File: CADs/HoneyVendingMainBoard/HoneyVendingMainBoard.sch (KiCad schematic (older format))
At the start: 31 parts, among them J1 SegmentPins, J2 CoinPins, J3 ConnToDoors, J4 12V Power, U1 L7805, U2 74HC165

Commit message: Update mainboard schematic
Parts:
- added 10kOhm? (x2): R, Resistor_SMD:R_0805_2012Metric_Pad1.15x1.40mm_HandSolder, symbol Device:R
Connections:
- net CoinSerial: now also 10kOhm?.1
- net GND: now also 10kOhm?.2, 10kOhm?.2
- net PISOOutput: now also 10kOhm?.1
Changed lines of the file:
@@
 	1    0    0    -1
 $EndComp
-Text Notes 3550 3500 0    50   ~ 0
+Text Notes 3550 3450 0    50   ~ 0
 Pins 2 and 3 are \ncapable of interrupts
 $Comp
@@
 	4350 3700 5100 3700
 Wire Wire Line
-	4350 3600 5100 3600
-Wire Wire Line
 	4350 3800 5100 3800
 Wire Wire Line
-	4350 3900 5100 3900
-Wire Wire Line
 	4350 4000 5100 4000
 Wire Wire Line
@@
 Wire Wire Line
 	4350 4600 5100 4600
-Text Label 4350 3600 0    50   ~ 0
+Text Label 4000 3600 0    50   ~ 0
 CoinSerial
 Text Label 4350 3700 0    50   ~ 0
@@
 Text Label 4350 3800 0    50   ~ 0
 PISOClock
-Text Label 4350 3900 0    50   ~ 0
+Text Label 3650 3900 0    50   ~ 0
 PISOOutput
 Text Label 4350 4000 0    50   ~ 0
@@
 Text Notes 4450 4650 0    20   ~ 0
 Pin 13 reserviert für Coin TX
+Wire Wire Line
+	4000 3600 4500 3600
+$Comp
+L Device:R 10kOhm?
+U 1 1 5E8354F3
+P 4300 3050
+F 0 "10kOhm?" V 4093 3050 50  0000 C CNN
+F 1 "R" V 4184 3050 50  0000 C CNN
+F 2 "Resistor_SMD:R_0805_2012Metric_Pad1.15x1.40mm_HandSolder" V 4230 3050 50  0001 C CNN
+F 3 "~" H 4300 3050 50  0001 C CNN
+	1    4300 3050
+	0    1    1    0
+$EndComp
+$Comp
+L power:GND #PWR?
+U 1 1 5E835551
+P 4000 3050
+F 0 "#PWR?" H 4000 2800 50  0001 C CNN
+F 1 "GND" H 4005 2877 50  0000 C CNN
+F 2 "" H 4000 3050 50  0001 C CNN
+F 3 "" H 4000 3050 50  0001 C CNN
+	1    4000 3050
+	0    1    1    0
+$EndComp
+Wire Wire Line
+	4150 3050 4000 3050
+Wire Wire Line
+	4450 3050 4500 3050
+Wire Wire Line
+	4500 3050 4500 3600
+Connection ~ 4500 3600
+Wire Wire Line
+	4500 3600 5100 3600
+$Comp
+L Device:R 10kOhm?
+U 1 1 5E8476D8
+P 3700 3700
+F 0 "10kOhm?" V 3493 3700 50  0000 C CNN
+F 1 "R" V 3584 3700 50  0000 C CNN
+F 2 "Resistor_SMD:R_0805_2012Metric_Pad1.15x1.40mm_HandSolder" V 3630 3700 50  0001 C CNN
+F 3 "~" H 3700 3700 50  0001 C CNN
+	1    3700 3700
+	0    1    1    0
+$EndComp
+$Comp
+L power:GND #PWR?
+U 1 1 5E847732
+P 3450 3700
+F 0 "#PWR?" H 3450 3450 50  0001 C CNN
+F 1 "GND" H 3455 3527 50  0000 C CNN
+F 2 "" H 3450 3700 50  0001 C CNN
+F 3 "" H 3450 3700 50  0001 C CNN
+	1    3450 3700
+	0    1    1    0
+$EndComp
+Wire Wire Line
+	3650 3900 4200 3900
+Wire Wire Line
+	3850 3700 4200 3700
+Wire Wire Line
+	4200 3700 4200 3900
+Connection ~ 4200 3900
+Wire Wire Line
+	4200 3900 5100 3900
+Wire Wire Line
+	3550 3700 3450 3700
 $EndSCHEMATC

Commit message: Reworded PCBs and added PCB pdfs
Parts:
- removed 10kOhm? (x2): R, Resistor_SMD:R_0805_2012Metric_Pad1.15x1.40mm_HandSolder, symbol Device:R
- added 100nF4: RCLKAntiFlicker, Capacitor_THT:C_Disc_D6.0mm_W2.5mm_P5.00mm, symbol Device:C
- 0.1µF1: value C -> VR3
- 0.33µF1: value C -> VR2
- 100nF1: value C -> ArduinoDecouple
- 100nF2: value C -> ButtonDecouple
- 100µF1: value C -> VR1
- 10kOhm1: value R -> CoinInhibitPullDown
- 10kOhm10: renamed from 10kOhm?; value R -> DoorClearPullUp
- 10kOhm2: value R -> ResetPD
- 10kOhm4: value R -> ButtonR4
- 10kOhm5: value R -> ButtonR5
- 10kOhm6: value R -> ButtonR6
- 10kOhm7: value R -> ButtonR2
- 10kOhm8: value R -> ButtonR3
- 10kOhm9: value R -> ButtonR1
- J2: footprint Connector_Molex:Molex_KK-254_AE-6410-05A_1x05_P2.54mm_Vertical -> Connector_PinHeader_2.54mm:PinHeader_1x05_P2.54mm_Vertical
- J3: footprint Connector_Molex:Molex_Mini-Fit_Jr_5566-08A_2x04_P4.20mm_Vertical -> Connector_PinHeader_2.54mm:PinHeader_2x04_P2.54mm_Vertical
- J4: footprint Connector_BarrelJack:BarrelJack_CUI_PJ-063AH_Horizontal -> Connector_BarrelJack:BarrelJack_Horizontal
- U1: footprint Package_TO_SOT_THT:TO-220F-3_Horizontal_TabDown -> Package_TO_SOT_THT:TO-220F-3_Vertical
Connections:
- net CoinSerial: now also A1.2 (D0/RX); no longer A1.6 (D3)
- net GND: now also 100nF4.1
- net doorRCLK: now also 100nF4.2
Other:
- note removed: "Pin 13 reserviert für Coin TX"

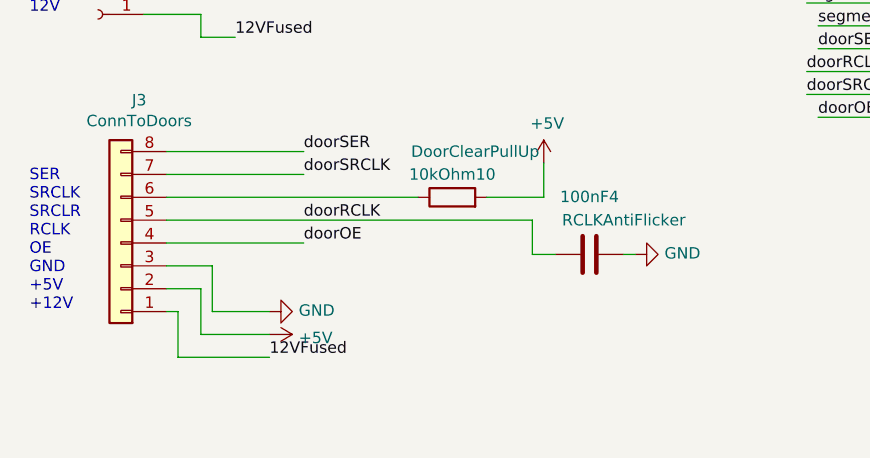
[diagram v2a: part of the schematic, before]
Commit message: Applying nicos feedback for boards
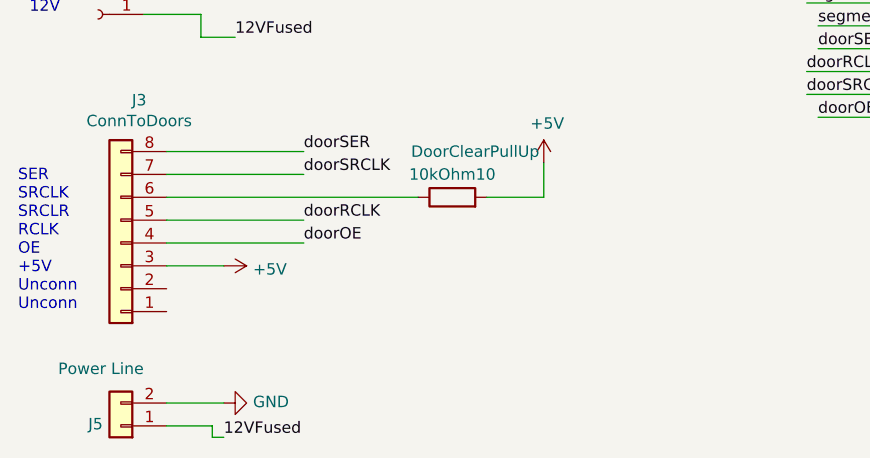
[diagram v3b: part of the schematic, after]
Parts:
- removed 100nF4: RCLKAntiFlicker, Capacitor_THT:C_Disc_D6.0mm_W2.5mm_P5.00mm, symbol Device:C
- added J5: Power Line, Connector_PinHeader_2.54mm:PinHeader_1x02_P2.54mm_Vertical, symbol Connector_Generic:Conn_01x02
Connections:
- net +5V: now also J3.3 (Pin_3); no longer J3.2 (Pin_2)
- net 12VFused: now also J5.1 (Pin_1); no longer J3.1 (Pin_1)
- net GND: now also J5.2 (Pin_2); no longer J3.3 (Pin_3)
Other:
- note added: "SER\nSRCLK\nSRCLR\nRCLK\nOE\n+5V\nUnconn\nUnconn"
- note removed: "SER\nSRCLK\nSRCLR\nRCLK\nOE\nGND\n+5V\n+12V"
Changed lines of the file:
@@
 	-1   0    0    1
 $EndComp
-Text Notes 550  5350 0    50   ~ 0
-SER\nSRCLK\nSRCLR\nRCLK\nOE\nGND\n+5V\n+12V
+Text Notes 500  5350 0    50   ~ 0
+SER\nSRCLK\nSRCLR\nRCLK\nOE\n+5V\nUnconn\nUnconn
 $Comp
 L power:GND #PWR0123
 U 1 1 5E80ACE6
-P 1600 5350
-F 0 "#PWR0123" H 1600 5100 50  0001 C CNN
-F 1 "GND" V 1605 5222 50  0000 R CNN
-F 2 "" H 1600 5350 50  0001 C CNN
-F 3 "" H 1600 5350 50  0001 C CNN
-	1    1600 5350
+P 1400 5750
+F 0 "#PWR0123" H 1400 5500 50  0001 C CNN
+F 1 "GND" V 1405 5622 50  0000 R CNN
+F 2 "" H 1400 5750 50  0001 C CNN
+F 3 "" H 1400 5750 50  0001 C CNN
+	1    1400 5750
 	0    -1   -1   0
 $EndComp
@@
 L power:+5V #PWR0124
 U 1 1 5E80AE41
-P 1600 5450
-F 0 "#PWR0124" H 1600 5300 50  0001 C CNN
-F 1 "+5V" V 1615 5578 50  0000 L CNN
-F 2 "" H 1600 5450 50  0001 C CNN
-F 3 "" H 1600 5450 50  0001 C CNN
-	1    1600 5450
+P 1400 5150
+F 0 "#PWR0124" H 1400 5000 50  0001 C CNN
+F 1 "+5V" V 1415 5278 50  0000 L CNN
+F 2 "" H 1400 5150 50  0001 C CNN
+F 3 "" H 1400 5150 50  0001 C CNN
+	1    1400 5150
 	0    1    1    0
 $EndComp
-Wire Wire Line
-	1150 5350 1200 5350
-Wire Wire Line
-	1200 5350 1200 5550
-Wire Wire Line
-	1200 5550 1600 5550
-Wire Wire Line
-	1600 5450 1300 5450
-Wire Wire Line
-	1300 5450 1300 5250
-Wire Wire Line
-	1300 5250 1150 5250
-Wire Wire Line
-	1150 5150 1350 5150
-Wire Wire Line
-	1350 5150 1350 5350
-Wire Wire Line
-	1350 5350 1600 5350
 Wire Wire Line
 	1750 4750 1150 4750
@@
 Text Label 1450 4150 0    50   ~ 0
 12VFused
-Text Label 1600 5550 0    50   ~ 0
+Text Label 1400 5900 0    50   ~ 0
 12VFused
 $Comp
@@
 Wire Wire Line
 	4550 3300 5100 3300
-$Comp
-L Device:C 100nF4
-U 1 1 5E93C28F
-P 3000 5100
-F 0 "100nF4" V 2748 5100 50  0000 C CNN
-F 1 "RCLKAntiFlicker" V 2850 5250 50  0000 C CNN
-F 2 "Capacitor_THT:C_Disc_D6.0mm_W2.5mm_P5.00mm" H 3038 4950 50  0001 C CNN
-F 3 "~" H 3000 5100 50  0001 C CNN
-	1    3000 5100
-	0    1    1    0
-$EndComp
-Wire Wire Line
-	2750 4950 2750 5100
-Wire Wire Line
-	2750 5100 2850 5100
-Wire Wire Line
-	1150 4950 2750 4950
-$Comp
-L power:GND #PWR0122
-U 1 1 5E944F2D
-P 3200 5100
-F 0 "#PWR0122" H 3200 4850 50  0001 C CNN
-F 1 "GND" V 3205 4972 50  0000 R CNN
-F 2 "" H 3200 5100 50  0001 C CNN
-F 3 "" H 3200 5100 50  0001 C CNN
-	1    3200 5100
-	0    -1   -1   0
-$EndComp
-Wire Wire Line
-	3150 5100 3200 5100
 Wire Wire Line
 	4900 2600 4900 2700
 Connection ~ 4900 2600
+Wire Wire Line
+	1150 5150 1400 5150
+$Comp
+L Connector_Generic:Conn_01x02 J5
+U 1 1 5E8EA156
+P 950 5850
+F 0 "J5" H 1029 5842 50  0000 L CNN
+F 1 "Power Line" H 850 5600 50  0000 L CNN
+F 2 "Connector_PinHeader_2.54mm:PinHeader_1x02_P2.54mm_Vertical" H 950 5850 50  0001 C CNN
+F 3 "~" H 950 5850 50  0001 C CNN
+	1    950  5850
+	-1   0    0    1
+$EndComp
+Wire Wire Line
+	1150 5850 1350 5850
+Wire Wire Line
+	1350 5850 1350 5900
+Wire Wire Line
+	1350 5900 1400 5900
+Wire Wire Line
+	1400 5750 1150 5750
+Wire Wire Line
+	1150 4950 1750 4950
 $EndSCHEMATC
